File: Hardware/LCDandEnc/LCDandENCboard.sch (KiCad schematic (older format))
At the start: 18 parts, among them J1 LCD4x20, J2 LCD4x20, U1 74HC14

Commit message: layout and BOM
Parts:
- removed J1: LCD4x20, Pin_Headers:Pin_Header_Straight_1x04_Pitch2.54mm, symbol Conn_01x04
- added C4: 1u, Capacitors_SMD:C_0805_HandSoldering, symbol C
- added C5: 100n, Capacitors_SMD:C_0805_HandSoldering, symbol C
- added J1: Connection to mainBoard, Pin_Headers:Pin_Header_Straight_1x07_Pitch2.54mm, symbol Conn_01x07_Female
- added U2: XC6206P332MR, TO_SOT_Packages_SMD:TSOT-23_HandSoldering, symbol XC6206P332MR
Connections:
- net GND: now also C4.2, C5.2, J1.1 (Pin_1), U2.1 (GND)
- net Rot_Enc_A: now also J1.3 (Pin_3)
- net Rot_Enc_B: now also U1.8, J1.2 (Pin_2); no longer U1.4
- net Rot_Enc_SW: now also J1.4 (Pin_4)
- net SCL: now also J1.5 (Pin_5)
- net SDA: now also J1.6 (Pin_6)
- net VCC: no longer 1U1.1, 1U2.1, J2.1 (Pin_1), R2.1, R3.1, R4.1
- net at C2.1, D2.1 (K), R5.2: now also U1.9; no longer U1.3
- new net +3V3: 1U1.1, 1U2.1, C5.1, R2.1, R3.1, R4.1, U2.2 (Vout)
- new net +5V: C4.1, J1.7 (Pin_7), J2.1 (Pin_1), U2.3 (Vin)
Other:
- moved on the sheet: 1U1

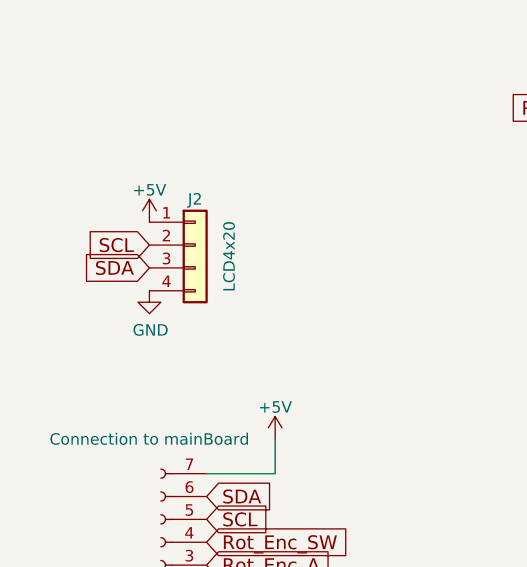
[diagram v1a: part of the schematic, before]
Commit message: Bad I2C pinout
Swappe some pins around to match the i2c lcd board
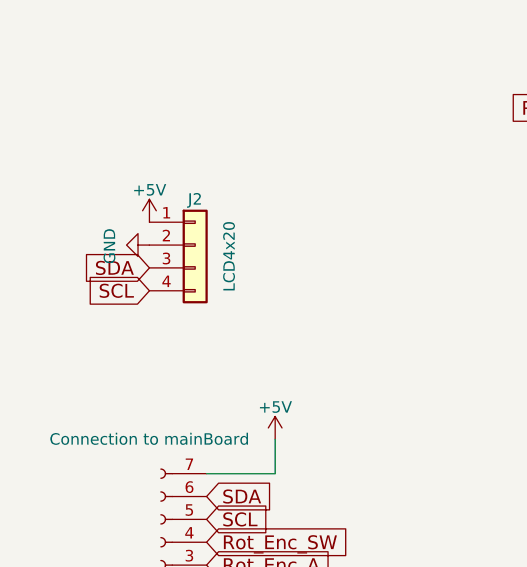
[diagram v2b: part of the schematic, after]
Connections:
- net GND: now also J2.2 (Pin_2); no longer J2.4 (Pin_4)
- net SCL: now also J2.4 (Pin_4); no longer J2.2 (Pin_2)
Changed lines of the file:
@@
 L GND #PWR03
 U 1 1 5A836804
-P 1600 4350
-F 0 "#PWR03" H 1600 4100 50  0001 C CNN
-F 1 "GND" H 1605 4177 50  0000 C CNN
-F 2 "" H 1600 4350 50  0001 C CNN
-F 3 "" H 1600 4350 50  0001 C CNN
-	1    1600 4350
-	1    0    0    -1
+P 1600 4150
+F 0 "#PWR03" H 1600 3900 50  0001 C CNN
+F 1 "GND" H 1605 3977 50  0000 C CNN
+F 2 "" H 1600 4150 50  0001 C CNN
+F 3 "" H 1600 4150 50  0001 C CNN
+	1    1600 4150
+	0    1    1    0
 $EndComp
-Text GLabel 1600 4150 0    60   Input ~ 0
+Text GLabel 1600 4350 0    60   Input ~ 0
 SCL
 Text GLabel 1600 4250 0    60   Input ~ 0
